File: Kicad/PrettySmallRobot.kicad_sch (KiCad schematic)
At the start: 54 parts, among them J1 TYPE-C-31-M-12, J2 S2B-PH-K-S(LF)(SN), J3 S2B-PH-K-S(LF)(SN), J4 S2B-PH-K-S(LF)(SN), SW1 SW_Push, U1 DRV8837, U2 DRV8837, U3 MCP73831-2ACI_MC

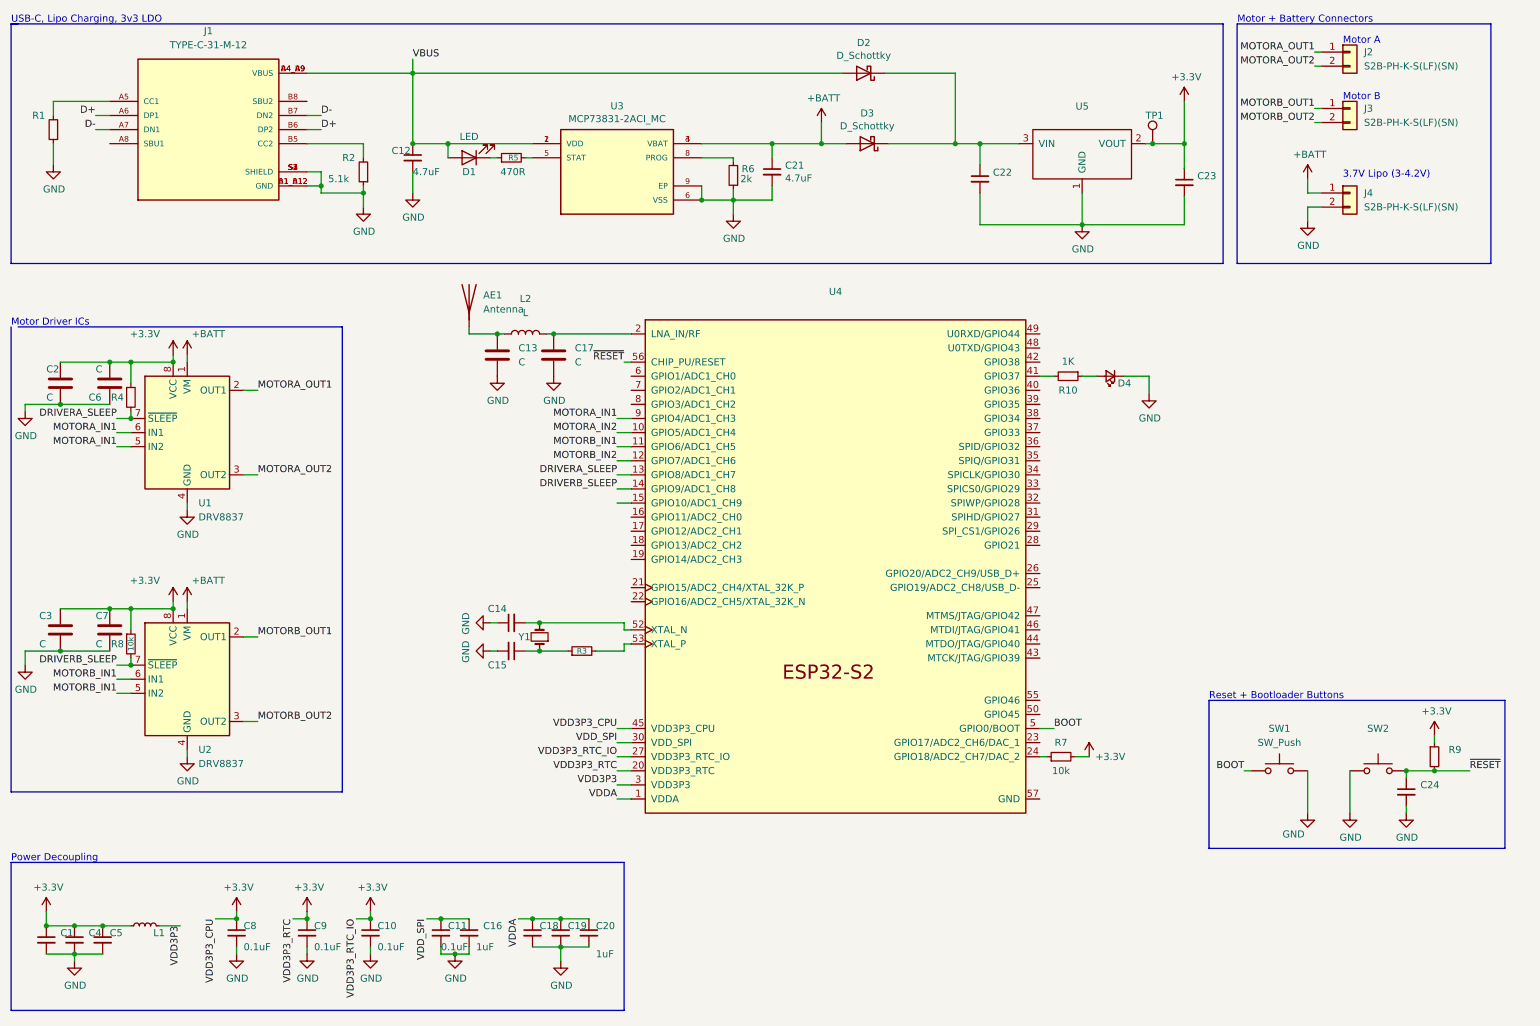
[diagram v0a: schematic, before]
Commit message: removed pullups on driver enable signals
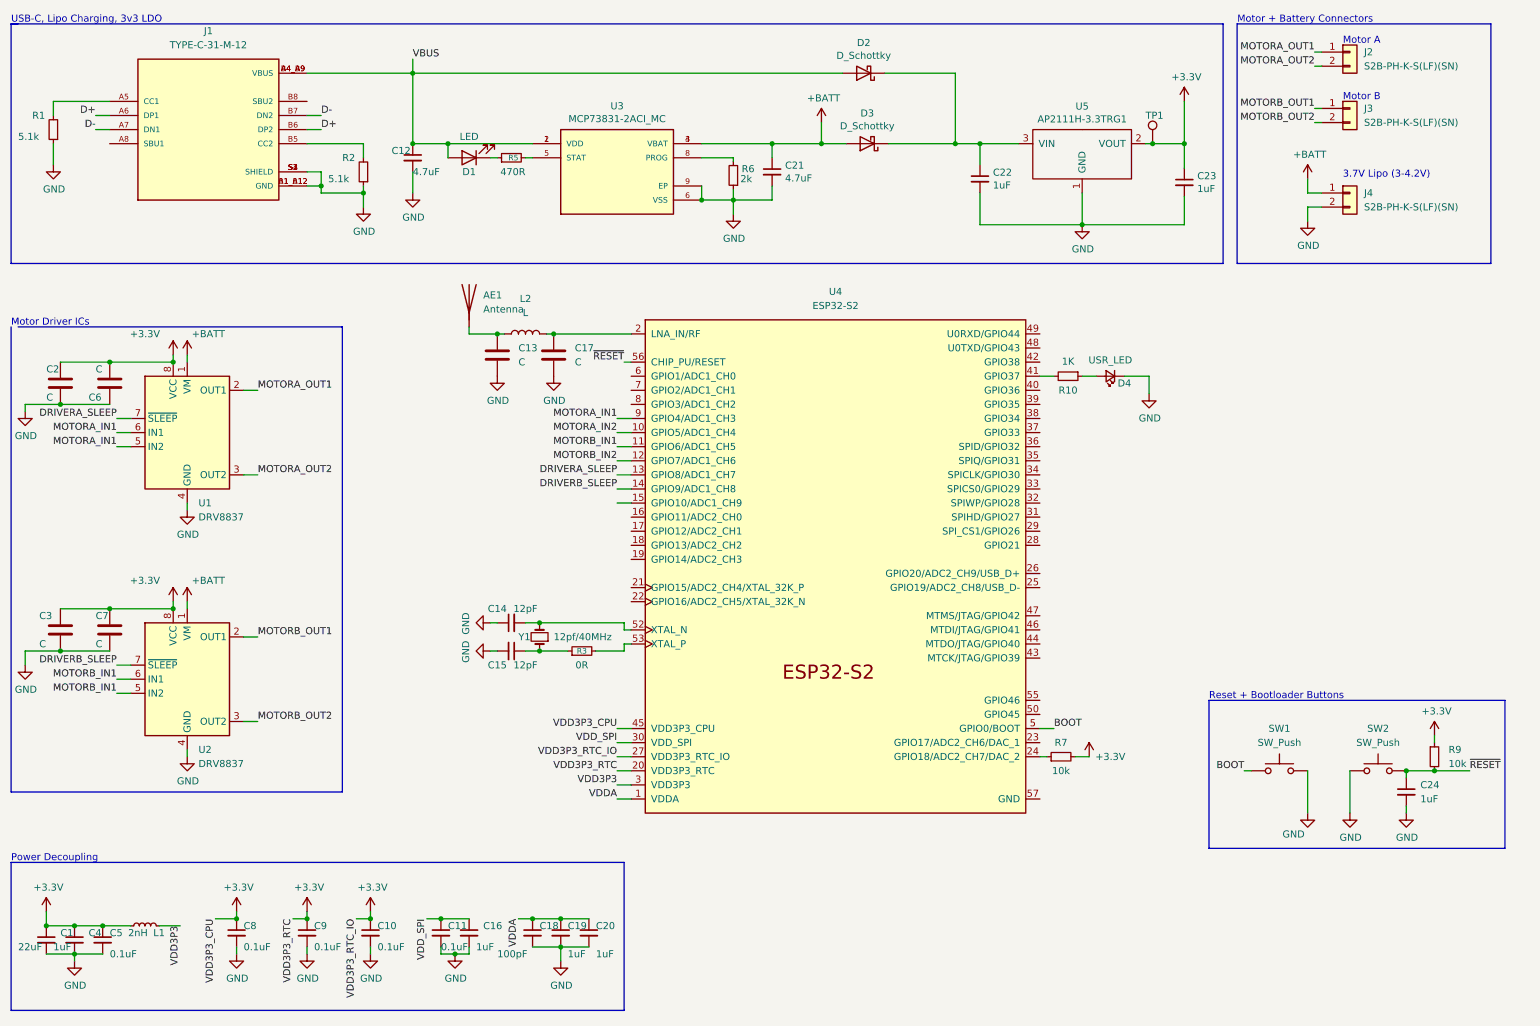
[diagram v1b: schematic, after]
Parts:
- removed R4: (no value), symbol Device:R_Small
- removed R8: 10k, symbol Device:R_Small
- C1: value (none) -> 22uF
- C14, C15: value (none) -> 12pF
- C18: value (none) -> 100pF
- C19, C22, C23, C24, C4: value (none) -> 1uF
- C5: value (none) -> 0.1uF
- D4: value (none) -> USR_LED
- L1: value (none) -> 2nH
- R1: value (none) -> 5.1k
- R3: value (none) -> 0R
- R9: value (none) -> 10k
- SW2: value (none) -> SW_Push
- TP1: value (none) -> TEST
- U3: footprint (none) -> kicad_footprints:SON50P200X300X100-9N
- U4: value (none) -> ESP32-S2; footprint (none) -> Package_DFN_QFN:QFN-56-1EP_7x7mm_P0.4mm_EP5.6x5.6mm
- U5: value (none) -> AP2111H-3.3TRG1
- Y1: value (none) -> 12pf/40MHz

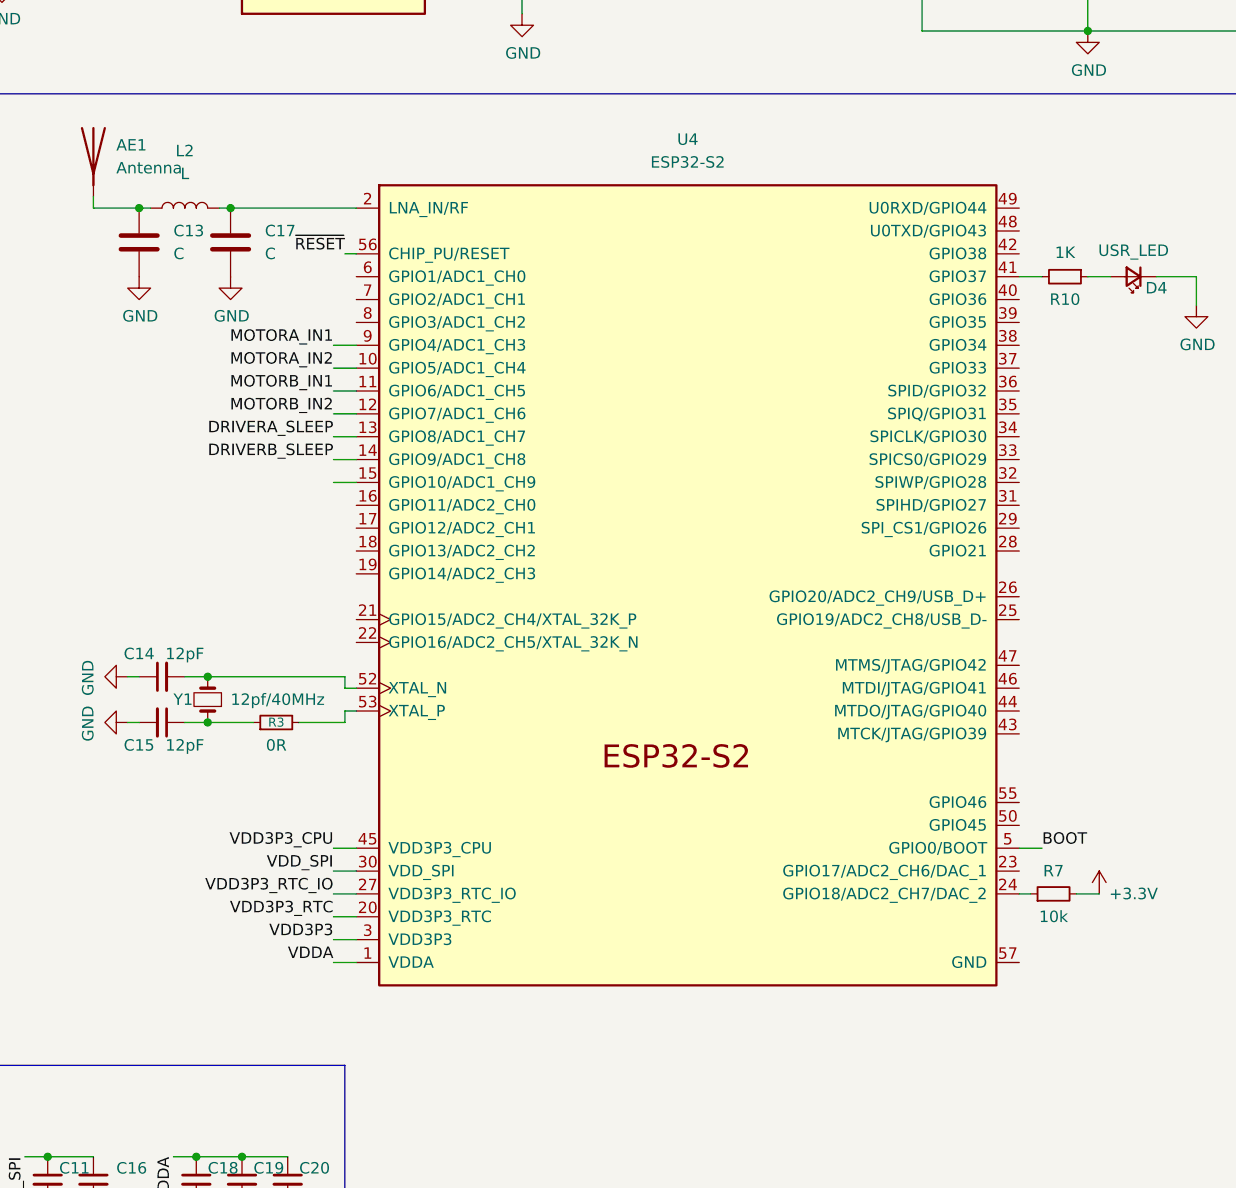
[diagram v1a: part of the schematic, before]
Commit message: added pi matching network vals + lcsc numbers
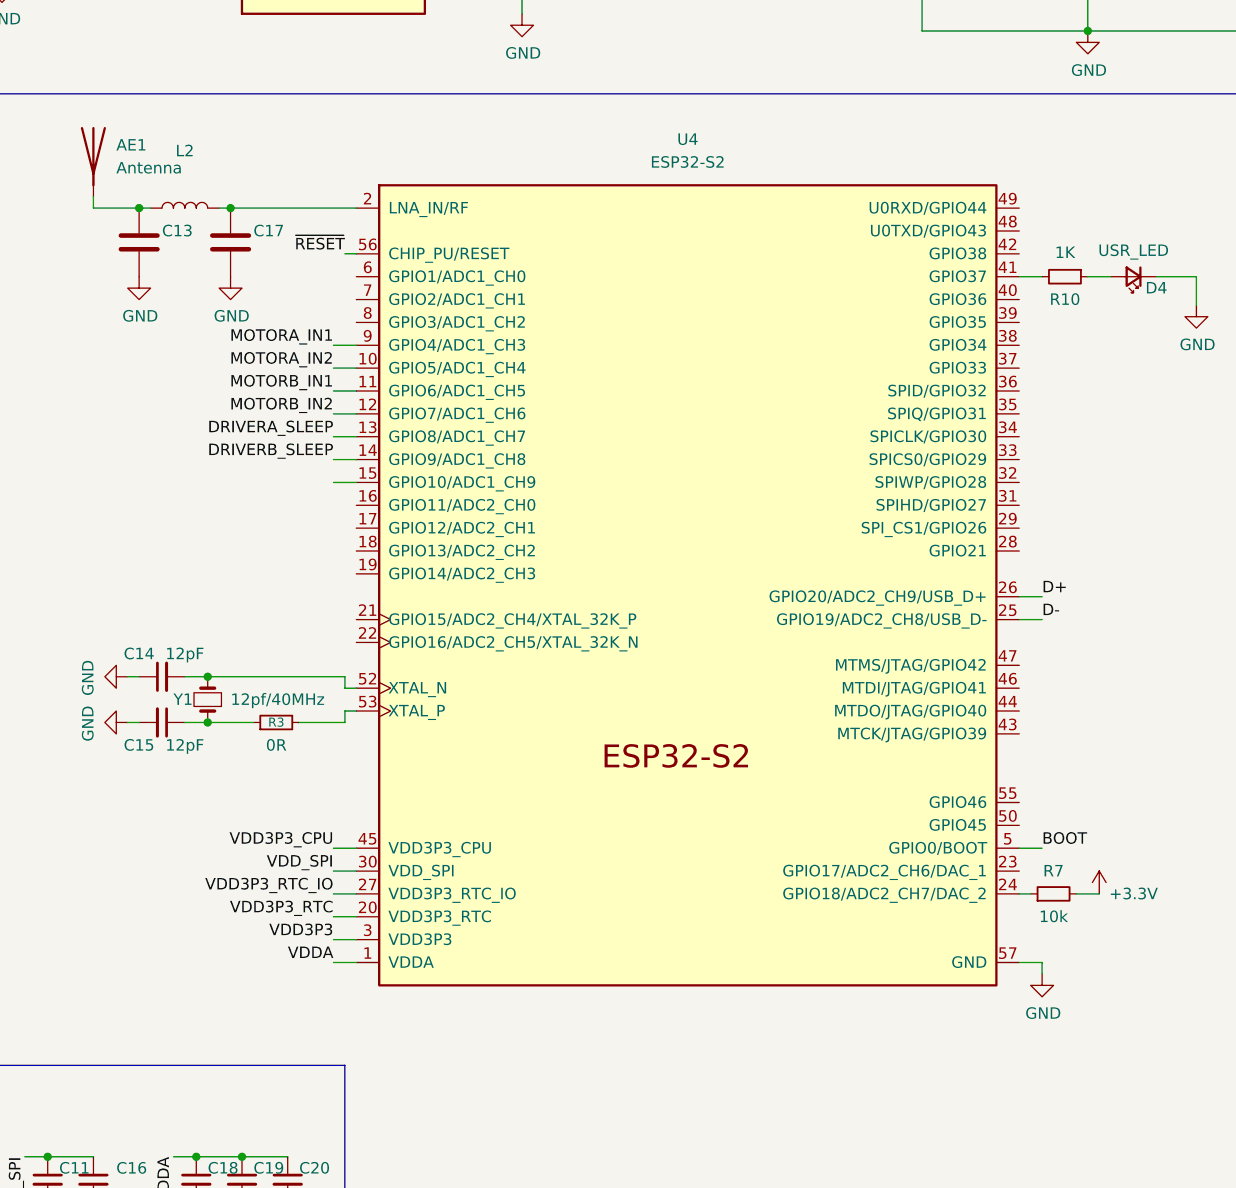
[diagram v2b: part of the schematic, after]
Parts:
- C13: value C -> (none); LCSC (none) -> C313081
- C17: value C -> (none); LCSC (none) -> C140677
- L2: value L -> (none); LCSC (none) -> C87530
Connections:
- net D+: now also U4.26 (GPIO20/ADC2_CH9/USB_D+)
- net D-: now also U4.25 (GPIO19/ADC2_CH8/USB_D-)
- net GND: now also U4.57 (GND)
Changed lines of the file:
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@@
+    (stroke (width 0) (type default) (color 0 0 0 0))
+  )
+  (wire (pts (xy 201.93 156.21) (xy 201.93 157.48))
     (stroke (width 0) (type default) (color 0 0 0 0))
   )
@@
     (stroke (width 0) (type default) (color 0 0 0 0))
   )
+  (wire (pts (xy 199.39 115.57) (xy 201.93 115.57))
+    (stroke (width 0) (type default) (color 0 0 0 0))
+  )
   (wire (pts (xy 250.19 49.53) (xy 247.65 49.53))
     (stroke (width 0) (type default) (color 0 0 0 0))
@@
     (stroke (width 0) (type default) (color 0 0 0 0))
   )
+  (wire (pts (xy 199.39 118.11) (xy 201.93 118.11))
+    (stroke (width 0) (type default) (color 0 0 0 0))
+  )
   (wire (pts (xy 144.145 46.355) (xy 144.145 48.26))
     (stroke (width 0) (type default) (color 0 0 0 0))
@@
   )
   (polyline (pts (xy 280.67 59.69) (xy 234.95 59.69))
+    (stroke (width 0) (type default) (color 0 0 0 0))
+  )
+  (wire (pts (xy 199.39 156.21) (xy 201.93 156.21))
     (stroke (width 0) (type default) (color 0 0 0 0))
   )
@@
     (effects (font (size 1.27 1.27)) (justify right bottom))
   )
+  (label "D+" (at 201.93 115.57 0)
+    (effects (font (size 1.27 1.27)) (justify left bottom))
+  )
   (label "VDD_SPI" (at 123.19 146.05 180)
     (effects (font (size 1.27 1.27)) (justify right bottom))
@@
     (effects (font (size 1.27 1.27)) (justify right bottom))
   )
+  (label "D-" (at 201.93 118.11 0)
+    (effects (font (size 1.27 1.27)) (justify left bottom))
+  )
   (label "MOTORB_IN1" (at 123.19 92.71 180)
     (effects (font (size 1.27 1.27)) (justify right bottom))
@@
     (pin "1")
     (pin "2")
+  )
+  (symbol (lib_id "power:GND") (at 201.93 157.48 0) (unit 1)
+    (in_bom yes) (on_board yes)
+    (property "Reference" "#PWR?" (id 0) (at 201.93 163.83 0)
+      (effects (font (size 1.27 1.27)) hide)
+    )
+    (property "Value" "GND" (id 1) (at 202.057 161.8742 0))
+    (property "Footprint" "" (id 2) (at 201.93 157.48 0)
+      (effects (font (size 1.27 1.27)) hide)
+    )
+    (property "Datasheet" "" (id 3) (at 201.93 157.48 0)
+      (effects (font (size 1.27 1.27)) hide)
+    )
+    (pin "1")
   )
   (symbol (lib_id "Device:C_Small") (at 25.4 181.61 0) (unit 1)
@@
   )
   (symbol (lib_id "Device:L") (at 106.68 72.39 90) (unit 1)
-    (in_bom yes) (on_board yes) (fields_autoplaced)
+    (in_bom yes) (on_board yes)
     (property "Reference" "L2" (id 0) (at 106.68 66.04 90))
-    (property "Value" "L" (id 1) (at 106.68 68.58 90))
+    (property "Value" "" (id 1) (at 106.68 69.85 90))
     (property "Footprint" "" (id 2) (at 106.68 72.39 0)
       (effects (font (size 1.27 1.27)) hide)
     )
     (property "Datasheet" "~" (id 3) (at 106.68 72.39 0)
+      (effects (font (size 1.27 1.27)) hide)
+    )
+    (property "LCSC" "C87530" (id 4) (at 106.68 72.39 0)
       (effects (font (size 1.27 1.27)) hide)
     )
@@
   )
   (symbol (lib_id "Device:C") (at 101.6 76.2 0) (unit 1)
-    (in_bom yes) (on_board yes) (fields_autoplaced)
-    (property "Reference" "C13" (id 0) (at 105.41 74.9299 0)
-      (effects (font (size 1.27 1.27)) (justify left))
-    )
-    (property "Value" "C" (id 1) (at 105.41 77.4699 0)
+    (in_bom yes) (on_board yes)
+    (property "Reference" "C13" (id 0) (at 104.14 74.93 0)
+      (effects (font (size 1.27 1.27)) (justify left))
+    )
+    (property "Value" "" (id 1) (at 104.14 77.47 0)
       (effects (font (size 1.27 1.27)) (justify left))
     )
@@
     )
     (property "Datasheet" "~" (id 3) (at 101.6 76.2 0)
+      (effects (font (size 1.27 1.27)) hide)
+    )
+    (property "LCSC" "C313081" (id 4) (at 101.6 76.2 0)
       (effects (font (size 1.27 1.27)) hide)
     )
@@
   )
   (symbol (lib_id "Device:C") (at 111.76 76.2 0) (unit 1)
-    (in_bom yes) (on_board yes) (fields_autoplaced)
-    (property "Reference" "C17" (id 0) (at 115.57 74.9299 0)
-      (effects (font (size 1.27 1.27)) (justify left))
-    )
-    (property "Value" "C" (id 1) (at 115.57 77.4699 0)
+    (in_bom yes) (on_board yes)
+    (property "Reference" "C17" (id 0) (at 114.3 74.93 0)
+      (effects (font (size 1.27 1.27)) (justify left))
+    )
+    (property "Value" "" (id 1) (at 114.3 78.74 0)
       (effects (font (size 1.27 1.27)) (justify left))
     )
@@
     )
     (property "Datasheet" "~" (id 3) (at 111.76 76.2 0)
+      (effects (font (size 1.27 1.27)) hide)
+    )
+    (property "LCSC" "    C140677" (id 4) (at 111.76 76.2 0)
       (effects (font (size 1.27 1.27)) hide)
     )
@@
       (reference "#PWR0137") (unit 1) (value "GND") (footprint "")
     )
+    (path "/0c8c8daf-98dd-4ccf-8dc1-56da5380353e"
+      (reference "#PWR?") (unit 1) (value "GND") (footprint "")
+    )
     (path "/d74a2731-c64a-407d-ada7-5d2cd3605482"
       (reference "AE1") (unit 1) (value "Antenna") (footprint "")
@@
     )
     (path "/46d4fead-ba21-4cf9-a4cd-802a72ed331f"
-      (reference "C13") (unit 1) (value "C") (footprint "")
+      (reference "C13") (unit 1) (value "3.9pF") (footprint "")
     )
     (path "/fded7505-6fce-4b81-90fd-219bd2c8e14c"
@@
     )
     (path "/b0d23ef2-2191-4783-b4e1-832a9d67dd65"
-      (reference "C17") (unit 1) (value "C") (footprint "")
+      (reference "C17") (unit 1) (value "1.8pF") (footprint "")
     )
     (path "/0baa52e2-c307-47ba-933b-c334a4b092c8"
@@
     )
     (path "/251ade2c-e1c8-4335-ab15-b1573b3e543c"
-      (reference "L2") (unit 1) (value "L") (footprint "")
+      (reference "L2") (unit 1) (value "1.8nH") (footprint "")
     )
     (path "/c2b6c29a-adcf-4ce5-9e2c-65b7d310e409"
